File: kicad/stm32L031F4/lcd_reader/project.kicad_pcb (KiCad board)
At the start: 2 copper layers, 24 x 43 mm, 22 parts, among them J1 WAKE, J13 GND_EXT, J2 SWD, J8 RADIO, Q1 CSD16414Q5, U1 74LS14, U2 STM32L031F4Px, U3 74LS14

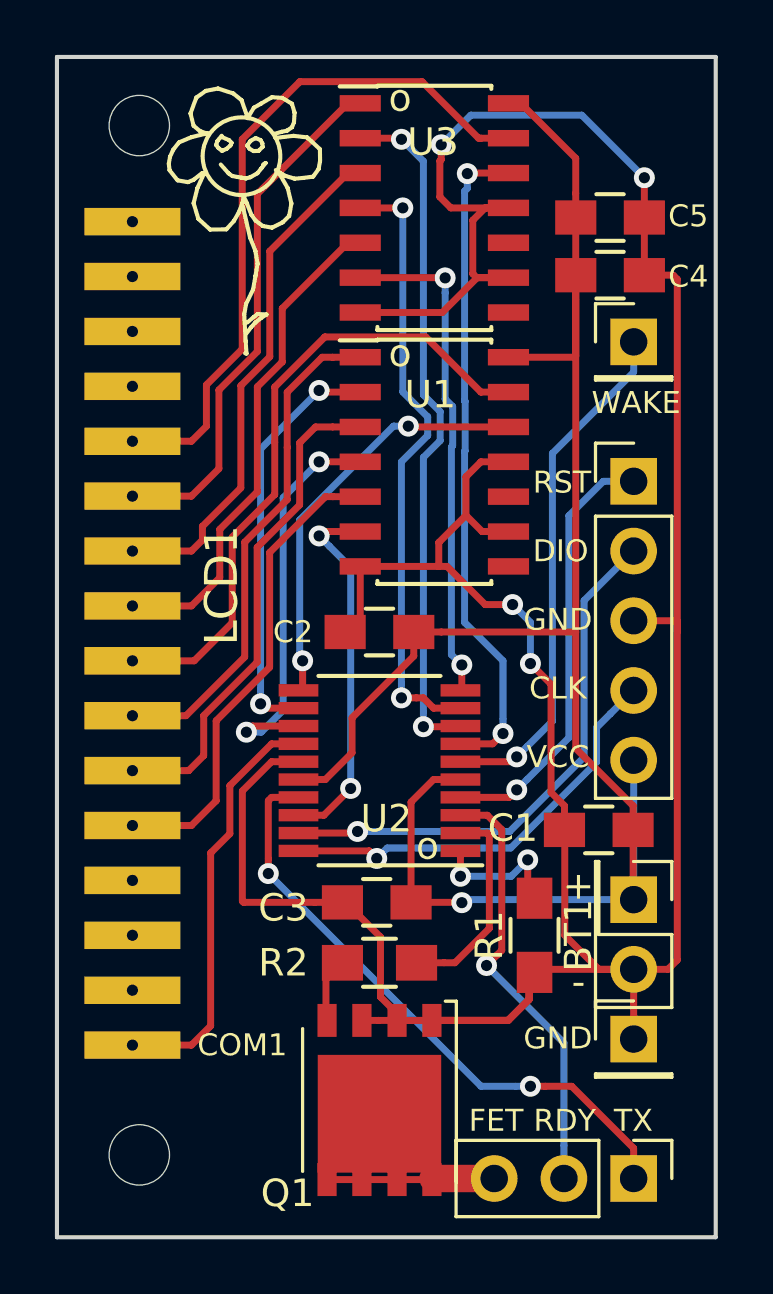
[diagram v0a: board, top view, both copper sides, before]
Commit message: Pull down on mosfet gate
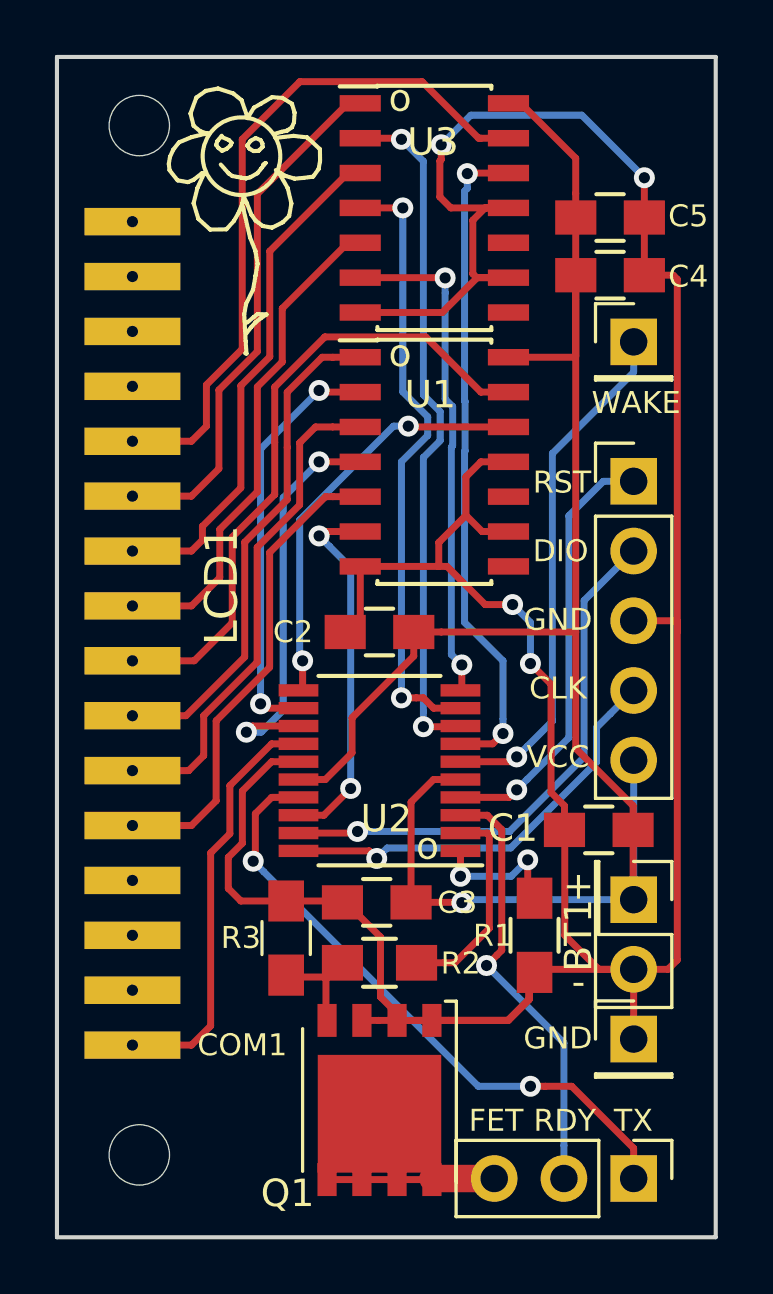
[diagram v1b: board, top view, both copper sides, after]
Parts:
- added R3: 10K, Resistors_SMD:R_0805_HandSoldering, F.Cu at (224.3, 125.6)
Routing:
- net Net-(Q1-Pad4): track 2.37 -> 4.66 mm
- net TX: track 22.4 -> 22.9 mm
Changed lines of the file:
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@@
 (kicad_pcb (version 4) (host pcbnew 4.0.7-e2-6376~58~ubuntu16.04.1)
   (general
-    (links 63)
+    (links 65)
     (no_connects 0)
     (area 215.924999 93.424999 240.075001 136.575001)
     (thickness 1.6)
     (drawings 23)
-    (tracks 363)
+    (tracks 369)
     (zones 0)
-    (modules 22)
+    (modules 23)
     (nets 41)
   )
@@
     (tags "resistor 0805")
     (attr smd)
-    (fp_text reference R2 (at -3.5 0) (layer F.SilkS)
-      (effects (font (size 1 1) (thickness 0.15)))
+    (fp_text reference R2 (at 2.96 0.02) (layer F.SilkS)
+      (effects (font (size 0.8 0.8) (thickness 0.15)))
     )
     (fp_text value 220R (at 0 2.1) (layer F.Fab)
@@
     (tags "capacitor 0805")
     (attr smd)
-    (fp_text reference C3 (at -3.4 0.2) (layer F.SilkS)
-      (effects (font (size 1 1) (thickness 0.15)))
+    (fp_text reference C3 (at 2.93 0.01) (layer F.SilkS)
+      (effects (font (size 0.8 0.8) (thickness 0.15)))
     )
     (fp_text value 0.1UF (at 0 2.1) (layer F.Fab)
@@
     (tags "resistor 0805")
     (attr smd)
-    (fp_text reference R1 (at 0 1.65 270) (layer F.SilkS)
-      (effects (font (size 1 1) (thickness 0.15)))
+    (fp_text reference R1 (at 0.01 1.51 360) (layer F.SilkS)
+      (effects (font (size 0.8 0.8) (thickness 0.15)))
     )
     (fp_text value 10K (at 0 2.1 270) (layer F.Fab)
@@
     )
   )
+  (module Resistors_SMD:R_0805_HandSoldering (layer F.Cu)
+    (at 224.35 125.6 90)
+    (descr "Resistor SMD 0805, hand soldering")
+    (tags "resistor 0805")
+    (attr smd)
+    (fp_text reference R3 (at 0.01 -1.65 180) (layer F.SilkS)
+      (effects (font (size 0.8 0.8) (thickness 0.15)))
+    )
+    (fp_text value 10K (at 0 1.75 90) (layer F.Fab)
+      (effects (font (size 1 1) (thickness 0.15)))
+    )
+    (fp_text user %R (at 0 0 90) (layer F.Fab)
+      (effects (font (size 0.5 0.5) (thickness 0.075)))
+    )
+    (fp_line (start -1 0.62) (end -1 -0.62) (layer F.Fab) (width 0.1))
+    (fp_line (start 1 0.62) (end -1 0.62) (layer F.Fab) (width 0.1))
+    (fp_line (start 1 -0.62) (end 1 0.62) (layer F.Fab) (width 0.1))
+    (fp_line (start -1 -0.62) (end 1 -0.62) (layer F.Fab) (width 0.1))
+    (fp_line (start 0.6 0.88) (end -0.6 0.88) (layer F.SilkS) (width 0.12))
+    (fp_line (start -0.6 -0.88) (end 0.6 -0.88) (layer F.SilkS) (width 0.12))
+    (fp_line (start -2.35 -0.9) (end 2.35 -0.9) (layer F.CrtYd) (width 0.05))
+    (fp_line (start -2.35 -0.9) (end -2.35 0.9) (layer F.CrtYd) (width 0.05))
+    (fp_line (start 2.35 0.9) (end 2.35 -0.9) (layer F.CrtYd) (width 0.05))
+    (fp_line (start 2.35 0.9) (end -2.35 0.9) (layer F.CrtYd) (width 0.05))
+    (pad 1 smd rect (at -1.35 0 90) (size 1.5 1.3) (layers F.Cu F.Paste F.Mask)
+      (net 21 "Net-(Q1-Pad4)"))
+    (pad 2 smd rect (at 1.35 0 90) (size 1.5 1.3) (layers F.Cu F.Paste F.Mask)
+      (net 2 GND))
+    (model ${KISYS3DMOD}/Resistors_SMD.3dshapes/R_0805.wrl
+      (at (xyz 0 0 0))
+      (scale (xyz 1 1 1))
+      (rotate (xyz 0 0 0))
+    )
+  )
   (gr_text o (at 228.5 95) (layer F.SilkS)
     (effects (font (size 1 1) (thickness 0.15)))
@@
   (segment (start 228.9 124.3) (end 228.9 120.646) (width 0.254) (layer F.Cu) (net 1))
   (segment (start 229.721 119.825) (end 230.7 119.825) (width 0.254) (layer F.Cu) (net 1))
+  (segment (start 224.8 119.175) (end 223.821 119.175) (width 0.254) (layer F.Cu) (net 2))
+  (segment (start 222.241999 123.791999) (end 222.7 124.25) (width 0.254) (layer F.Cu) (net 2))
+  (segment (start 223.821 119.175) (end 222.754011 120.241989) (width 0.254) (layer F.Cu) (net 2))
+  (segment (start 222.241999 122.660159) (end 222.241999 123.791999) (width 0.254) (layer F.Cu) (net 2))
+  (segment (start 222.754011 120.241989) (end 222.754011 122.148147) (width 0.254) (layer F.Cu) (net 2))
+  (segment (start 222.754011 122.148147) (end 222.241999 122.660159) (width 0.254) (layer F.Cu) (net 2))
+  (segment (start 222.7 124.25) (end 224.35 124.25) (width 0.254) (layer F.Cu) (net 2))
+  (segment (start 224.35 124.25) (end 226.35 124.25) (width 0.254) (layer F.Cu) (net 2))
+  (segment (start 226.35 124.25) (end 226.4 124.3) (width 0.254) (layer F.Cu) (net 2))
   (segment (start 237.4 101.45) (end 238.45 101.45) (width 0.254) (layer F.Cu) (net 2))
   (segment (start 238.45 101.45) (end 238.6 101.6) (width 0.254) (layer F.Cu) (net 2))
   (segment (start 238.6 101.6) (end 238.6 114.427919) (width 0.254) (layer F.Cu) (net 2))
-  (segment (start 225.396 124.3) (end 226.4 124.3) (width 0.254) (layer F.Cu) (net 2))
-  (segment (start 223.821 119.175) (end 222.754011 120.241989) (width 0.254) (layer F.Cu) (net 2))
-  (segment (start 222.754011 124.254011) (end 222.8 124.3) (width 0.254) (layer F.Cu) (net 2))
-  (segment (start 224.8 119.175) (end 223.821 119.175) (width 0.254) (layer F.Cu) (net 2))
-  (segment (start 222.8 124.3) (end 225.396 124.3) (width 0.254) (layer F.Cu) (net 2))
-  (segment (start 222.754011 120.241989) (end 222.754011 124.254011) (width 0.254) (layer F.Cu) (net 2))
   (segment (start 234.49 121.66) (end 234.5 121.67) (width 0.254) (layer F.Cu) (net 2))
   (segment (start 234.5 121.67) (end 234.5 125.5) (width 0.254) (layer F.Cu) (net 2))
@@
   (via (at 228.8 106.95) (size 0.762) (drill 0.4064) (layers F.Cu B.Cu) (net 11))
   (segment (start 232.45 106.98) (end 232 106.98) (width 0.254) (layer F.Cu) (net 11))
+  (segment (start 223.227211 122.722789) (end 223.15 122.8) (width 0.254) (layer F.Cu) (net 12))
+  (segment (start 223.821 120.475) (end 223.227211 121.068789) (width 0.254) (layer F.Cu) (net 12))
+  (segment (start 223.227211 121.068789) (end 223.227211 122.722789) (width 0.254) (layer F.Cu) (net 12))
+  (segment (start 223.530999 123.180999) (end 223.15 122.8) (width 0.254) (layer B.Cu) (net 12))
+  (segment (start 224.8 120.475) (end 223.821 120.475) (width 0.254) (layer F.Cu) (net 12))
+  (segment (start 231.35 131) (end 223.530999 123.180999) (width 0.254) (layer B.Cu) (net 12))
+  (segment (start 233.25 131) (end 231.35 131) (width 0.254) (layer B.Cu) (net 12))
+  (via (at 223.15 122.8) (size 0.762) (drill 0.4064) (layers F.Cu B.Cu) (net 12))
   (segment (start 233.788815 131) (end 233.25 131) (width 0.254) (layer F.Cu) (net 12))
   (segment (start 234.754 131) (end 233.788815 131) (width 0.254) (layer F.Cu) (net 12))
   (segment (start 237.01 133.256) (end 234.754 131) (width 0.254) (layer F.Cu) (net 12))
   (segment (start 237.01 134.36) (end 237.01 133.256) (width 0.254) (layer F.Cu) (net 12))
-  (segment (start 231.449998 131) (end 232.711185 131) (width 0.254) (layer B.Cu) (net 12))
-  (segment (start 223.7 123.250002) (end 231.449998 131) (width 0.254) (layer B.Cu) (net 12))
-  (segment (start 232.711185 131) (end 233.25 131) (width 0.254) (layer B.Cu) (net 12))
   (via (at 233.25 131) (size 0.762) (drill 0.4064) (layers F.Cu B.Cu) (net 12))
-  (segment (start 223.7 122.711187) (end 223.7 123.250002) (width 0.254) (layer F.Cu) (net 12))
-  (segment (start 223.821 120.475) (end 223.7 120.596) (width 0.254) (layer F.Cu) (net 12))
-  (segment (start 224.8 120.475) (end 223.821 120.475) (width 0.254) (layer F.Cu) (net 12))
-  (via (at 223.7 123.250002) (size 0.762) (drill 0.4064) (layers F.Cu B.Cu) (net 12))
-  (segment (start 223.7 120.596) (end 223.7 122.711187) (width 0.254) (layer F.Cu) (net 12))
   (segment (start 234.47 133.157919) (end 234.47 134.36) (width 0.254) (layer B.Cu) (net 13))
   (segment (start 234.47 129.42) (end 234.47 133.157919) (width 0.254) (layer B.Cu) (net 13))
@@
   (segment (start 231.679 121.775) (end 231.752001 121.848001) (width 0.254) (layer F.Cu) (net 20))
   (segment (start 230.7 121.775) (end 231.679 121.775) (width 0.254) (layer F.Cu) (net 20))
+  (segment (start 224.35 126.95) (end 224.42 127.02) (width 0.254) (layer F.Cu) (net 21))
+  (segment (start 224.42 127.02) (end 225.88 127.02) (width 0.254) (layer F.Cu) (net 21))
+  (segment (start 225.88 127.02) (end 226.4 126.5) (width 0.254) (layer F.Cu) (net 21))
   (segment (start 226.4 126.5) (end 225.8 127.1) (width 0.254) (layer F.Cu) (net 21))
   (segment (start 225.8 127.1) (end 225.8 128.56) (width 0.254) (layer F.Cu) (net 21))
